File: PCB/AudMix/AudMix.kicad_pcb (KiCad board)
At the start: 2 copper layers, 100 x 90 mm, 84 parts, among them J1 Conn_01x03_Socket, J2 Conn_01x03_Socket, J3 Conn_01x03_Pin, Q1 PMOS, SW1 SW_SP3T, U1 ESP32-C3-SuperMini-left, U10 SSD1315, U2 TP4056, U3 AP1117-33, U4 DW01A, U5 FS8205A, U6 SSD1315, U7 SSD1315, U8 SSD1315, U9 SSD1315

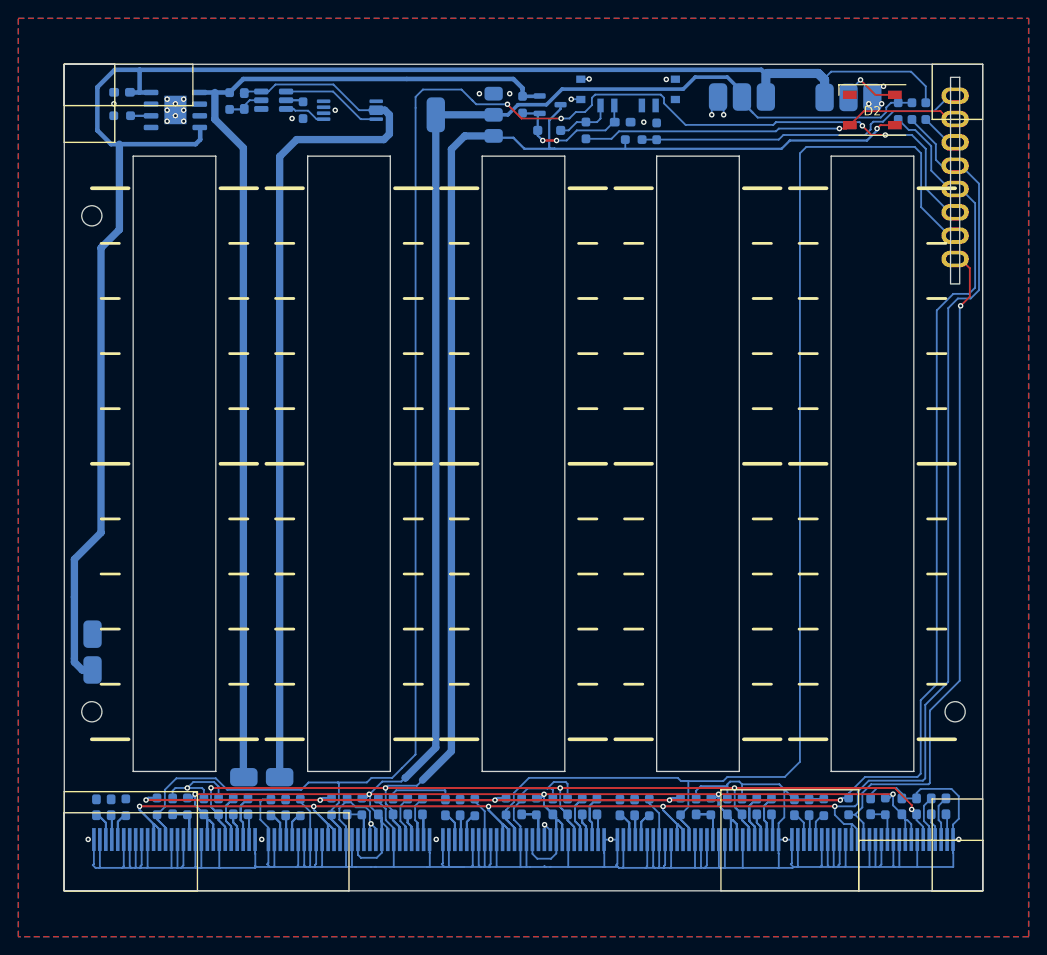
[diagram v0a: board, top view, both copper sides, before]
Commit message: PCB production ready
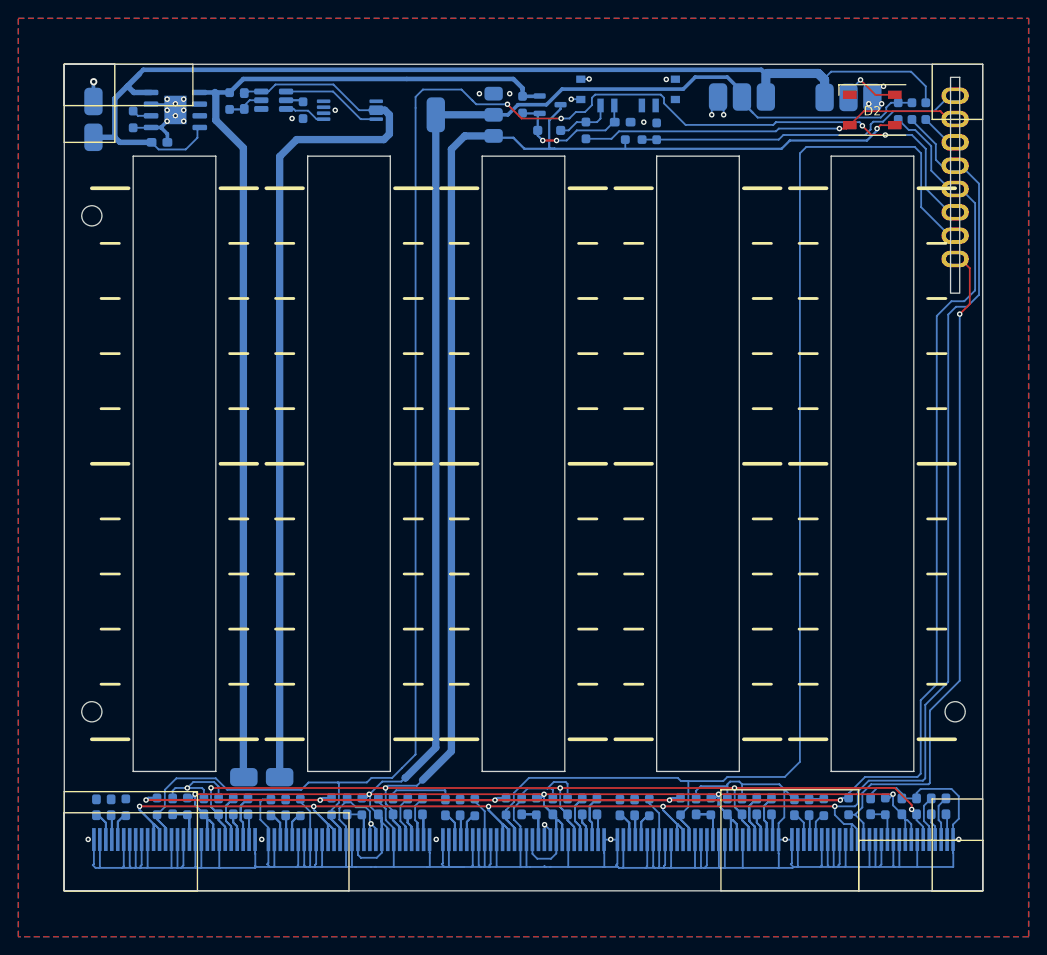
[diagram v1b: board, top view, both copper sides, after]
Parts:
- added REF**: OSHW-Logo2_7.3x6mm_SilkScreen, Symbol:OSHW-Logo2_7.3x6mm_SilkScreen, B.Cu at (71.5, 60.0)
- moved J3 58.0 mm to (53.5, 56.0)
- moved C1 6.81 mm to (60.4, 58.5), turned to 0 degrees
- moved R3 1.26 mm to (57.5, 56.0), turned to -90 degrees
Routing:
- net +5V: track 183.2 -> 118.9 mm
- net GND: track 424.0 -> 435.2 mm
